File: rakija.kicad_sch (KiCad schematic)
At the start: 0 parts

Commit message: added some components
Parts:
- added D1, D2, D3, D4, D5, D6: LED, LED_SMD:LED_0603_1608Metric_Pad1.05x0.95mm_HandSolder, symbol Device:LED
- added J1: Conn_02x03_Odd_Even, Connector_IDC:IDC-Header_2x03_P2.54mm_Vertical_SMD, symbol Connector_Generic:Conn_02x03_Odd_Even
- added R1, R2, R3, R4, R5, R6: TBD, Resistor_SMD:R_0603_1608Metric_Pad0.98x0.95mm_HandSolder, symbol Device:R_US
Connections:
- new net: D2.2 (A), R2.2
- new net: D4.2 (A), R4.2
- new net: D5.2 (A), R5.2
- new net: D6.2 (A), R6.2
- new net: D1.2 (A), R1.2
- new net: D3.2 (A), R3.2
- new net +3V0: J1.1 (Pin_1), R1.1, R2.1, R3.1, R4.1, R5.1, R6.1
- new net GND: D1.1 (K), D2.1 (K), D3.1 (K), D4.1 (K), D5.1 (K), D6.1 (K), J1.2 (Pin_2)
- no-connect marks 0 -> 4

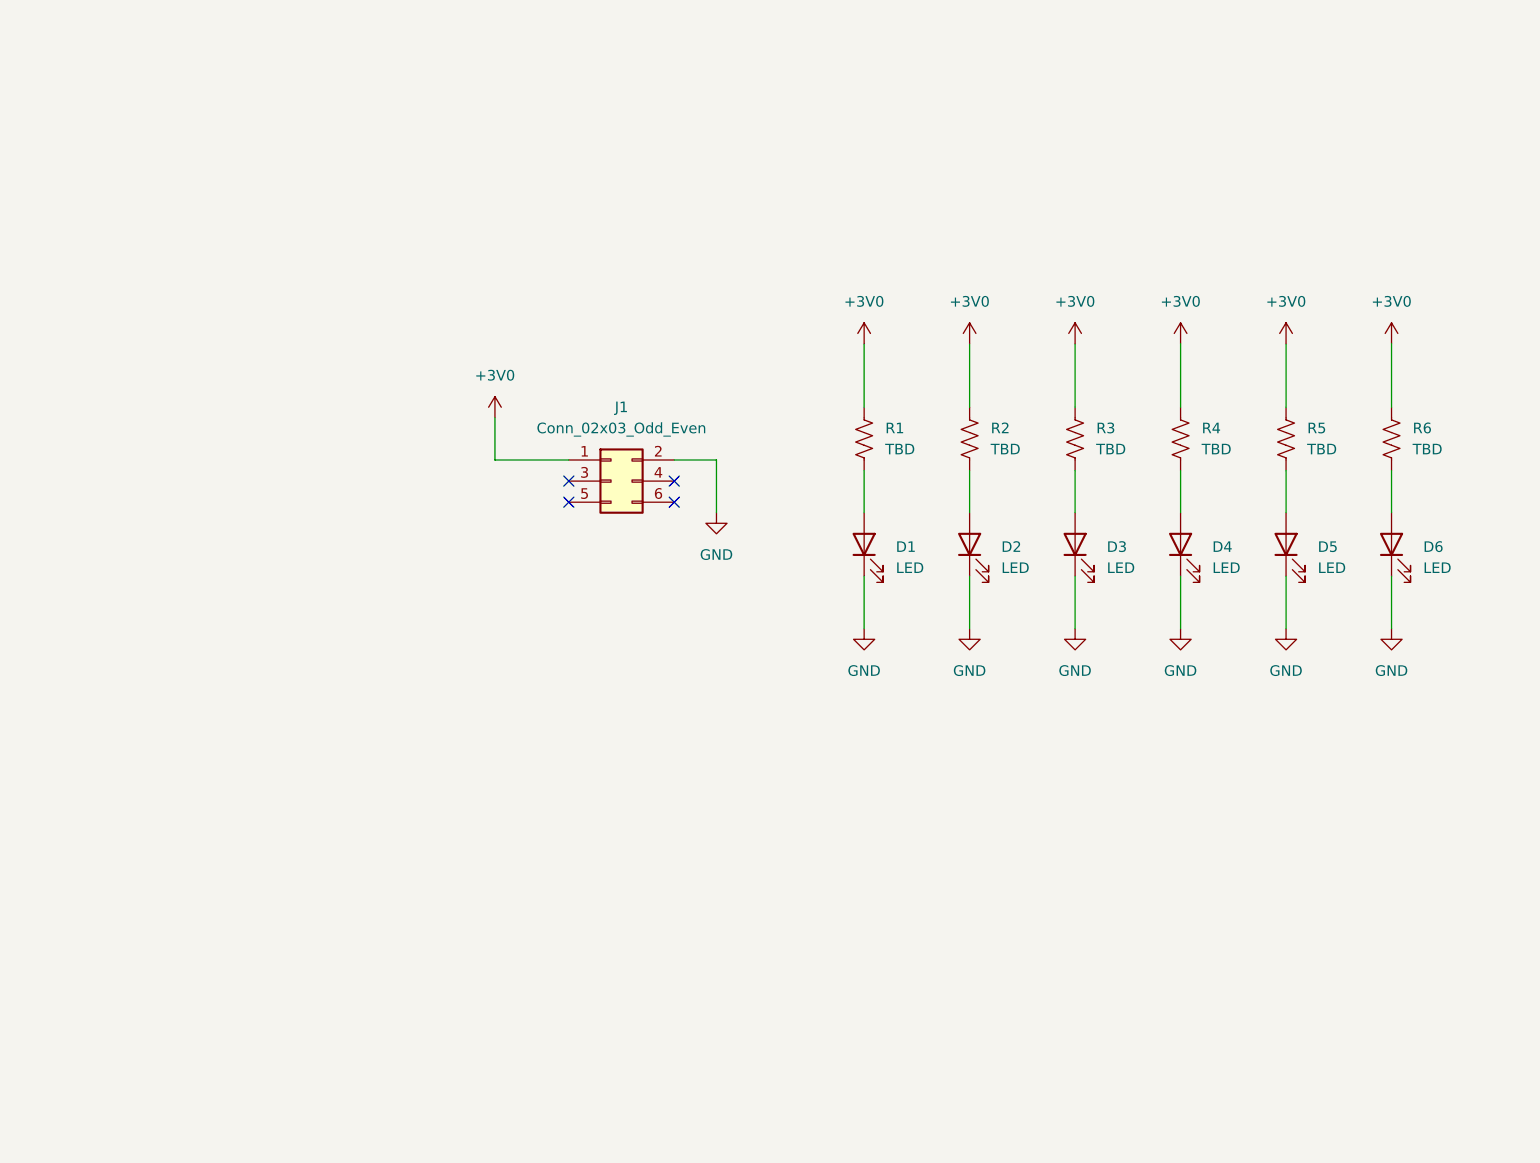
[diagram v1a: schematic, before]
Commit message: leds routed
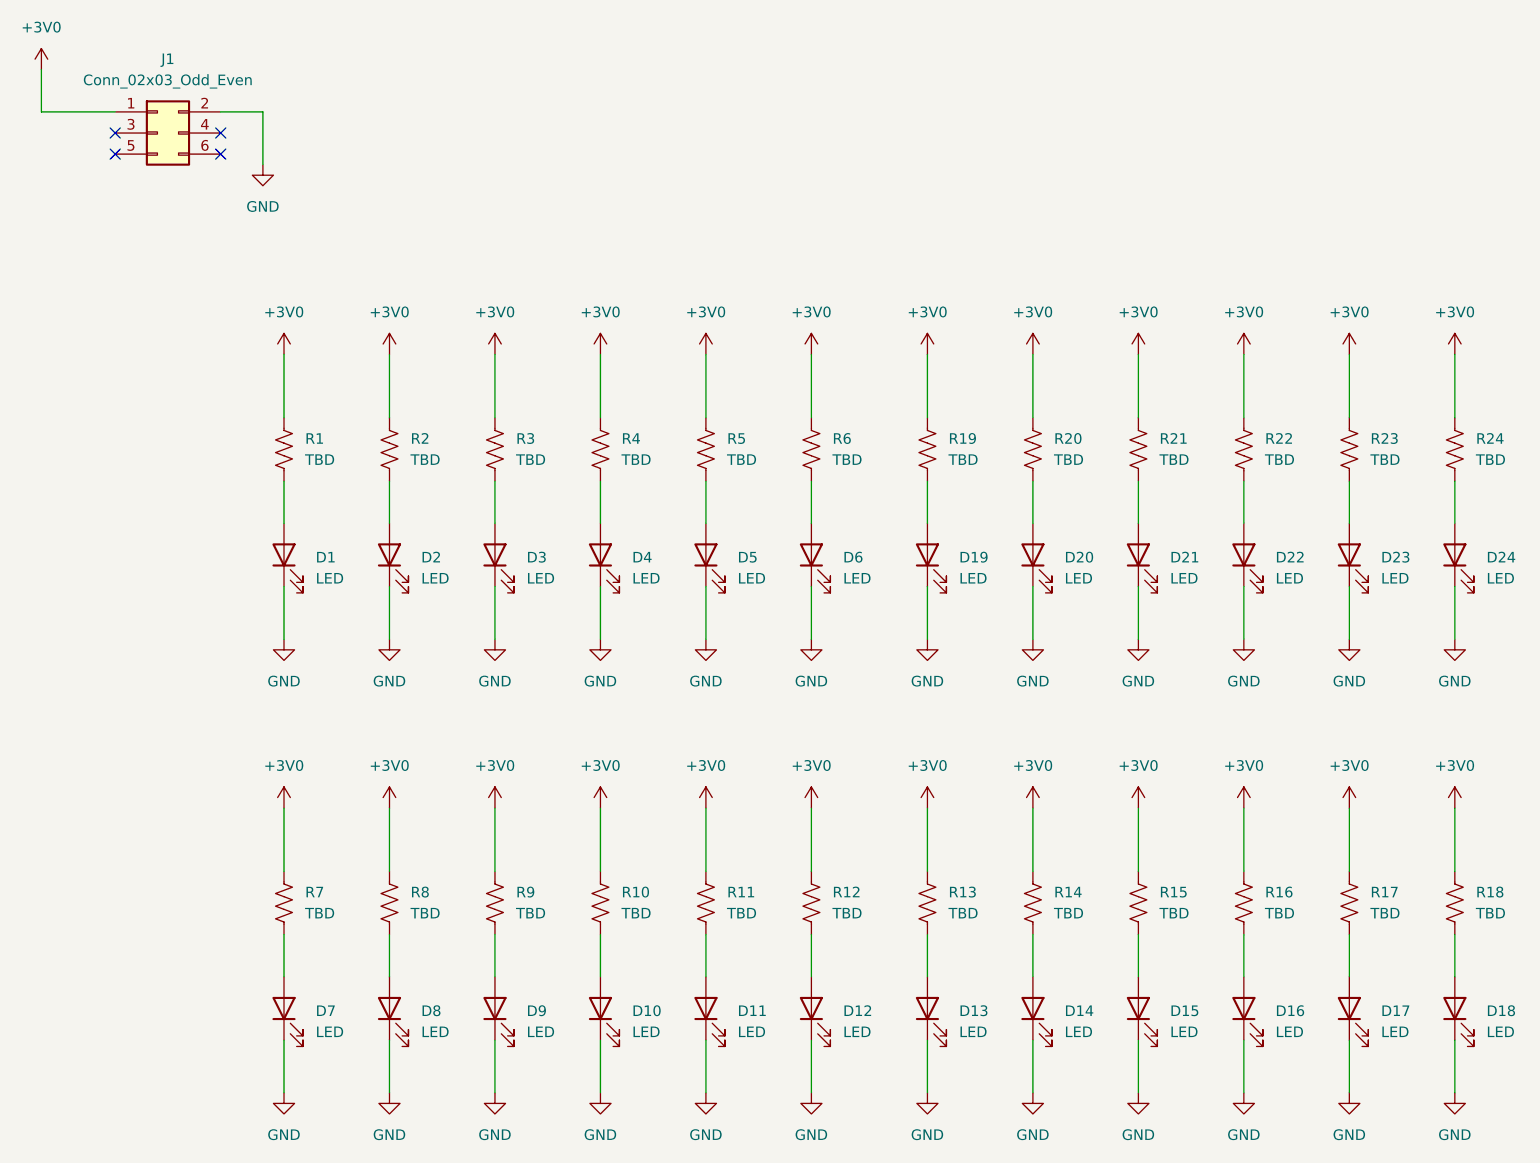
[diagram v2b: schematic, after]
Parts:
- added D10, D11, D12, D13, D14, D15, D16, D17, D18, D19, D20, D21, D22, D23, D24, D7, D8, D9: LED, LED_SMD:LED_0603_1608Metric_Pad1.05x0.95mm_HandSolder, symbol Device:LED
- added R10, R11, R12, R13, R14, R15, R16, R17, R18, R19, R20, R21, R22, R23, R24, R7, R8, R9: TBD, Resistor_SMD:R_0603_1608Metric_Pad0.98x0.95mm_HandSolder, symbol Device:R_US
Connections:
- net +3V0: now also R10.1, R11.1, R12.1, R13.1, R14.1, R15.1, R16.1, R17.1, R18.1, R19.1, R20.1, R21.1, R22.1, R23.1, R24.1, R7.1, R8.1, R9.1
- net GND: now also D10.1 (K), D11.1 (K), D12.1 (K), D13.1 (K), D14.1 (K), D15.1 (K), D16.1 (K), D17.1 (K), D18.1 (K), D19.1 (K), D20.1 (K), D21.1 (K), D22.1 (K), D23.1 (K), D24.1 (K), D7.1 (K), D8.1 (K), D9.1 (K)
- new net: D21.2 (A), R21.2
- new net: D20.2 (A), R20.2
- new net: D15.2 (A), R15.2
- new net: D23.2 (A), R23.2
- new net: D10.2 (A), R10.2
- new net: D19.2 (A), R19.2
- new net: D7.2 (A), R7.2
- new net: D12.2 (A), R12.2
- new net: D22.2 (A), R22.2
- new net: D18.2 (A), R18.2
- new net: D24.2 (A), R24.2
- new net: D9.2 (A), R9.2
- new net: D16.2 (A), R16.2
- new net: D13.2 (A), R13.2
- new net: D17.2 (A), R17.2
- new net: D11.2 (A), R11.2
- new net: D14.2 (A), R14.2
- new net: D8.2 (A), R8.2
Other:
- moved on the sheet: D1, D2, D3, D4, D5, D6, J1, R1, R2, R3, R4, R5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
